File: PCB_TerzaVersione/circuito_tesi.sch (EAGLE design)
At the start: 57 parts, among them IC1 SCD41-D-R2, Q1 BSS138, Q2 BSS138, Q3 BSS138, Q4 BSS138, U3 MICS-6814, U6 BME280, U7 LIS3DH, Y1 ECS-.327-9-16-TR

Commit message: Colleganenti PCB fatti
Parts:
- removed U7: LIS3DH, LIS3DH:LIS3DH
- added U1: STMICROELECTRONICS_LIS3DHSTMICROELECTRONICS_LIS3DH_0_0, STMicroelectronics - LIS3DH:STMICROELECTRONICS_LIS3DHSTMICROELECTRONICS_LIS3DH_0_0
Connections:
- new net BATTERY: C9.1, MDBT42Q.P0.31/AIN7, R19.2, R20.2
- net 3.3V: now also U1.CS, U1.VDD, U1.VDD_IO; no longer U7.CS, U7.VDD, U7.VDD_IO
- net AIN4: no longer C9.1, R19.2, R20.2
- net GND: now also U1.1_GND, U1.2_GND, U1.RES, U1.SA0/SDO; no longer U7.GND, U7.GND1, U7.RES, U7.SDO/SA0
- net P8: no longer MDBT42Q.P0.25
- net SCL: now also U1.SCL/SPC; no longer U7.SCL/SPC
- net SDA: now also U1.SDA/SDI/SDO; no longer U7.SDA/SDI/SDO

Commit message: Connessioni OK
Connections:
- removed net AIN4: MDBT42Q.P0.28/AIN4
- net P8: now also MDBT42Q.P0.27
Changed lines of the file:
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@@
-</segment>
-</net>
-<net name="AIN4" class="0">
-<segment>
-<pinref part="MDBT42Q" gate="G$1" pin="P0.28/AIN4"/>
-<wire x1="-149.86" y1="25.4" x2="-134.62" y2="25.4" width="0.1524" layer="91"/>
-<label x="-134.62" y="25.4" size="1.778" layer="95" xref="yes"/>
 </segment>
 </net>
@@
 <label x="43.18" y="246.38" size="1.778" layer="95" rot="R180" xref="yes"/>
 </segment>
+<segment>
+<pinref part="MDBT42Q" gate="G$1" pin="P0.27"/>
+<wire x1="-149.86" y1="27.94" x2="-144.78" y2="27.94" width="0.1524" layer="91"/>
+<label x="-144.78" y="27.94" size="1.778" layer="95" xref="yes"/>
+</segment>
 </net>

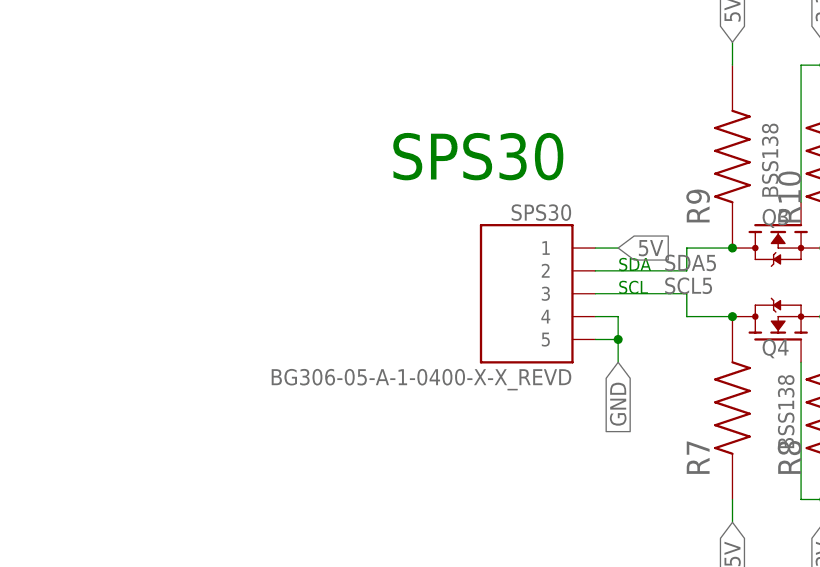
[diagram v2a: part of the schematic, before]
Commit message: Cambiato piedino SPS30
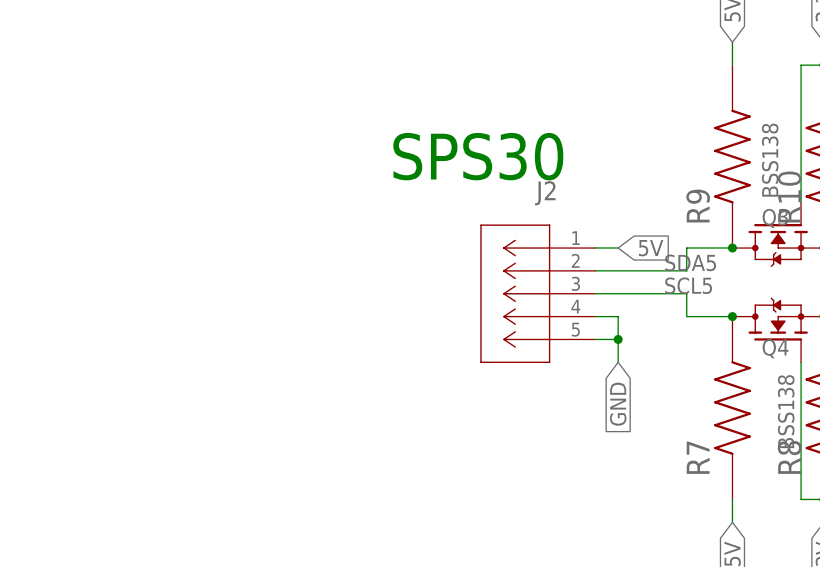
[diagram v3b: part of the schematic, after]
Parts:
- removed SPS30: BG306-05-A-1-0400-X-X_REVD, Connet_5_BG306-05-A-1-0400-X-X_REVD:BG306-05-A-1-0400-X-X_REVD
- added J2: S5B-ZR-SM4A-TF_(LF)_(SN)CONN_S5B-ZR-SM4A-TF_JST, CONN_SMD_5PIN:S5B-ZR-SM4A-TF_(LF)_(SN)CONN_S5B-ZR-SM4A-TF_JST
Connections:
- net 5V: now also J2.1; no longer SPS30.1
- net GND: now also J2.4, J2.5; no longer SPS30.4, SPS30.5
- net SCL5: now also J2.3; no longer SPS30.3
- net SDA5: now also J2.2; no longer SPS30.2
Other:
- note removed: "SCL"
- note removed: "SDA"
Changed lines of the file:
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@@
 <part name="GND1" library="SparkFun-PowerSymbols" deviceset="GND" device=""/>
 <part name="Y1" library="Crystal-ECS-.327-9-16-TR" deviceset="ECS-.327-9-16-TR" device=""/>
-<part name="SPS30" library="Connet_5_BG306-05-A-1-0400-X-X_REVD" deviceset="BG306-05-A-1-0400-X-X_REVD" device=""/>
 <part name="PROGRAMMER" library="Connet_6_BG306-04-A-1-0400-X-X_REVD" deviceset="BG306-04-A-1-0400-X-X_REVD" device=""/>
 <part name="GND3" library="supply" deviceset="GND" device=""/>
@@
 <part name="C13" library="Condensatore_case_0402" deviceset="C0402H102J5GACTU" device=""/>
 <part name="U1" library="STMicroelectronics - LIS3DH" deviceset="STMICROELECTRONICS_LIS3DH" device="STMICROELECTRONICS_LIS3DH_0_0"/>
+<part name="J2" library="CONN_SMD_5PIN" deviceset="S5B-ZR-SM4A-TF_(LF)_(SN)" device="CONN_S5B-ZR-SM4A-TF_JST"/>
 </parts>
 <sheets>
 <sheet>
 <plain>
-<text x="-302.26" y="200.66" size="1.4224" layer="91">SCL</text>
-<text x="-302.26" y="203.2" size="1.4224" layer="91">SDA</text>
 <text x="-231.902" y="220.472" size="5.08" layer="91">SCD41</text>
 <text x="-327.66" y="213.36" size="5.08" layer="91">SPS30</text>
@@
 <attribute name="VALUE" x="-236.210609375" y="50.790609375" size="1.781290625" layer="96" rot="R90"/>
 </instance>
-<instance part="SPS30" gate="G$1" x="-312.42" y="200.66" smashed="yes" rot="MR0">
-<attribute name="NAME" x="-307.34" y="208.788" size="1.778" layer="95" rot="MR0"/>
-<attribute name="VALUE" x="-307.34" y="190.5" size="1.778" layer="96" rot="MR0"/>
-</instance>
 <instance part="PROGRAMMER" gate="G$1" x="-358.14" y="-15.24" smashed="yes" rot="MR0">
 <attribute name="NAME" x="-353.051440625" y="-7.0983" size="1.781" layer="95" rot="MR0"/>
@@
 <instance part="U1" gate="G$0" x="-213.36" y="144.78" smashed="yes">
 <attribute name="NAME" x="-213.36" y="142.24" size="2.54" layer="95" align="top-left"/>
+</instance>
+<instance part="J2" gate="A" x="-304.8" y="205.74" smashed="yes" rot="MR0">
+<attribute name="NAME" x="-308.9646" y="211.0486" size="2.083" layer="95" ratio="6" rot="MR0"/>
 </instance>
 </instances>
@@
 <segment>
 <label x="-302.26" y="205.74" size="1.778" layer="95" xref="yes"/>
-<pinref part="SPS30" gate="G$1" pin="1"/>
 <wire x1="-304.8" y1="205.74" x2="-302.26" y2="205.74" width="0.1524" layer="91"/>
+<pinref part="J2" gate="A" pin="1"/>
 </segment>
 <segment>
@@
 <wire x1="-294.64" y1="203.2" x2="-294.64" y2="205.74" width="0.1524" layer="91"/>
 <wire x1="-294.64" y1="205.74" x2="-289.56" y2="205.74" width="0.1524" layer="91"/>
-<pinref part="SPS30" gate="G$1" pin="2"/>
 <label x="-297.18" y="203.2" size="1.778" layer="95"/>
 <pinref part="R9" gate="G$1" pin="1"/>
 <junction x="-289.56" y="205.74"/>
+<pinref part="J2" gate="A" pin="2"/>
 </segment>
 </net>
@@
 <wire x1="-302.26" y1="195.58" x2="-302.26" y2="193.04" width="0.1524" layer="91"/>
 <label x="-302.26" y="193.04" size="1.778" layer="95" rot="R270" xref="yes"/>
-<pinref part="SPS30" gate="G$1" pin="4"/>
 <wire x1="-304.8" y1="198.12" x2="-302.26" y2="198.12" width="0.1524" layer="91"/>
-<pinref part="SPS30" gate="G$1" pin="5"/>
 <wire x1="-304.8" y1="195.58" x2="-302.26" y2="195.58" width="0.1524" layer="91"/>
+<pinref part="J2" gate="A" pin="4"/>
+<pinref part="J2" gate="A" pin="5"/>
 </segment>
 <segment>
@@
 <wire x1="-294.64" y1="198.12" x2="-289.56" y2="198.12" width="0.1524" layer="91"/>
 <pinref part="Q4" gate="G$1" pin="D"/>
-<pinref part="SPS30" gate="G$1" pin="3"/>
 <label x="-297.18" y="200.66" size="1.778" layer="95"/>
 <pinref part="R7" gate="G$1" pin="2"/>
 <junction x="-289.56" y="198.12"/>
-</segment>
-</net>
+<pinref part="J2" gate="A" pin="3"/>
+</segment>
+</net>

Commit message: Prototipo finale
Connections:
- net 3.3V: now also C5.1, V_R_1.8.ON_/_OFF, V_R_1.8.VIN
- net VDD: no longer C5.1, V_R_1.8.ON_/_OFF, V_R_1.8.VIN
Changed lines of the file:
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@@
-</segment>
-<segment>
-<label x="35.56" y="-12.7" size="1.778" layer="95" rot="R180" xref="yes"/>
-<pinref part="V_R_1.8" gate="G$1" pin="VIN"/>
-<wire x1="45.72" y1="-12.7" x2="38.1" y2="-12.7" width="0.1524" layer="91"/>
-<pinref part="C5" gate="G$1" pin="1"/>
-<wire x1="38.1" y1="-12.7" x2="35.56" y2="-12.7" width="0.1524" layer="91"/>
-<junction x="38.1" y="-12.7"/>
 </segment>
 <segment>
@@
 <junction x="45.72" y="35.56"/>
 <label x="43.18" y="35.56" size="1.778" layer="95" rot="R180" xref="yes"/>
-</segment>
-<segment>
-<pinref part="V_R_1.8" gate="G$1" pin="ON_/_OFF"/>
-<wire x1="45.72" y1="-17.78" x2="45.72" y2="-20.32" width="0.1524" layer="91"/>
-<label x="45.72" y="-20.32" size="1.778" layer="95" rot="R270" xref="yes"/>
 </segment>
 <segment>
@@
 <wire x1="-220.98" y1="111.76" x2="-218.44" y2="111.76" width="0.1524" layer="91"/>
 </segment>
+<segment>
+<pinref part="V_R_1.8" gate="G$1" pin="VIN"/>
+<wire x1="45.72" y1="-12.7" x2="38.1" y2="-12.7" width="0.1524" layer="91"/>
+<pinref part="C5" gate="G$1" pin="1"/>
+<wire x1="38.1" y1="-12.7" x2="30.48" y2="-12.7" width="0.1524" layer="91"/>
+<junction x="38.1" y="-12.7"/>
+<label x="30.48" y="-12.7" size="1.778" layer="95" rot="R180" xref="yes"/>
+</segment>
+<segment>
+<pinref part="V_R_1.8" gate="G$1" pin="ON_/_OFF"/>
+<wire x1="45.72" y1="-17.78" x2="45.72" y2="-22.86" width="0.1524" layer="91"/>
+<label x="45.72" y="-22.86" size="1.778" layer="95" rot="R270" xref="yes"/>
+</segment>
 </net>

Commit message: Cambiato collegamento BJT
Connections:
- net 5V: now also OPAMP.VCC+, R11.1, R12.1; no longer BJT.C
- net BJT: now also BJT.C, U3.RH1/RS1_OX, U3.RH1/RS1_RED; no longer BJT.E, OPAMP.VCC+, R11.1, R12.1
- net GND: now also BJT.E; no longer U3.RH1/RS1_OX, U3.RH1/RS1_RED
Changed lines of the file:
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@@
 <part name="U1" library="STMicroelectronics - LIS3DH" deviceset="STMICROELECTRONICS_LIS3DH" device="STMICROELECTRONICS_LIS3DH_0_0"/>
 <part name="J2" library="CONN_SMD_5PIN" deviceset="S5B-ZR-SM4A-TF_(LF)_(SN)" device="CONN_S5B-ZR-SM4A-TF_JST"/>
+<part name="GND11" library="supply" deviceset="GND" device=""/>
 </parts>
 <sheets>
@@
 <attribute name="NAME" x="-308.9646" y="211.0486" size="2.083" layer="95" ratio="6" rot="MR0"/>
 </instance>
+<instance part="GND11" gate="1" x="83.82" y="236.22" smashed="yes">
+<attribute name="VALUE" x="81.28" y="233.68" size="1.778" layer="96"/>
+</instance>
 </instances>
 <busses>
@@
 </segment>
 <segment>
-<pinref part="BJT" gate="G$1" pin="C"/>
-<wire x1="83.82" y1="251.46" x2="83.82" y2="256.54" width="0.1524" layer="91"/>
-<label x="83.82" y="256.54" size="1.778" layer="95" rot="R90" xref="yes"/>
+<pinref part="OPAMP" gate="A" pin="VCC+"/>
+<wire x1="71.12" y1="200.66" x2="73.66" y2="200.66" width="0.1524" layer="91"/>
+<label x="73.66" y="200.66" size="1.778" layer="95" xref="yes"/>
+</segment>
+<segment>
+<pinref part="R11" gate="G$1" pin="1"/>
+<wire x1="170.18" y1="187.96" x2="172.72" y2="187.96" width="0.1524" layer="91"/>
+<label x="172.72" y="187.96" size="1.778" layer="95" xref="yes"/>
+</segment>
+<segment>
+<pinref part="R12" gate="G$1" pin="1"/>
+<wire x1="96.52" y1="226.06" x2="96.52" y2="228.6" width="0.1524" layer="91"/>
+<label x="96.52" y="228.6" size="1.778" layer="95" rot="R90" xref="yes"/>
 </segment>
 </net>
@@
 <wire x1="71.12" y1="182.88" x2="73.66" y2="182.88" width="0.1524" layer="91"/>
 <label x="73.66" y="182.88" size="1.778" layer="95" xref="yes"/>
-</segment>
-<segment>
-<pinref part="U3" gate="G$1" pin="RH1/RS1_RED"/>
-<wire x1="147.32" y1="203.2" x2="149.86" y2="203.2" width="0.1524" layer="91"/>
-<label x="149.86" y="203.2" size="1.778" layer="95" xref="yes"/>
-</segment>
-<segment>
-<pinref part="U3" gate="G$1" pin="RH1/RS1_OX"/>
-<wire x1="101.6" y1="187.96" x2="99.06" y2="187.96" width="0.1524" layer="91"/>
-<label x="99.06" y="187.96" size="1.778" layer="95" rot="R180" xref="yes"/>
 </segment>
 <segment>
@@
 <junction x="-180.34" y="114.3"/>
 </segment>
+<segment>
+<pinref part="BJT" gate="G$1" pin="E"/>
+<wire x1="83.82" y1="241.3" x2="83.82" y2="238.76" width="0.1524" layer="91"/>
+<pinref part="GND11" gate="1" pin="GND"/>
+</segment>
 </net>
 <net name="N$11" class="0">
@@
 <junction x="-241.3" y="50.8"/>
 <pinref part="C13" gate="G$1" pin="1"/>
-</segment>
-</net>
-<net name="BJT" class="0">
-<segment>
-<pinref part="BJT" gate="G$1" pin="E"/>
-<wire x1="83.82" y1="241.3" x2="83.82" y2="238.76" width="0.1524" layer="91"/>
-<label x="83.82" y="238.76" size="1.778" layer="95" rot="R270" xref="yes"/>
-</segment>
-<segment>
-<pinref part="R12" gate="G$1" pin="1"/>
-<wire x1="96.52" y1="226.06" x2="96.52" y2="228.6" width="0.1524" layer="91"/>
-<label x="96.52" y="228.6" size="1.778" layer="95" rot="R90" xref="yes"/>
-</segment>
-<segment>
-<pinref part="R11" gate="G$1" pin="1"/>
-<wire x1="170.18" y1="187.96" x2="172.72" y2="187.96" width="0.1524" layer="91"/>
-<label x="172.72" y="187.96" size="1.778" layer="95" xref="yes"/>
-</segment>
-<segment>
-<pinref part="OPAMP" gate="A" pin="VCC+"/>
-<wire x1="71.12" y1="200.66" x2="73.66" y2="200.66" width="0.1524" layer="91"/>
-<label x="73.66" y="200.66" size="1.778" layer="95" xref="yes"/>
 </segment>
 </net>
@@
 </segment>
 </net>
+<net name="BJT" class="0">
+<segment>
+<pinref part="U3" gate="G$1" pin="RH1/RS1_RED"/>
+<wire x1="147.32" y1="203.2" x2="149.86" y2="203.2" width="0.1524" layer="91"/>
+<label x="149.86" y="203.2" size="1.778" layer="95" xref="yes"/>
+</segment>
+<segment>
+<pinref part="U3" gate="G$1" pin="RH1/RS1_OX"/>
+<wire x1="101.6" y1="187.96" x2="99.06" y2="187.96" width="0.1524" layer="91"/>
+<label x="99.06" y="187.96" size="1.778" layer="95" rot="R180" xref="yes"/>
+</segment>
+<segment>
+<pinref part="BJT" gate="G$1" pin="C"/>
+<wire x1="83.82" y1="251.46" x2="83.82" y2="254" width="0.1524" layer="91"/>
+<label x="83.82" y="254" size="1.778" layer="95" rot="R90" xref="yes"/>
+</segment>
+</net>

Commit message: Resistenze con valore esatto
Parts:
- removed LED1: LTST-C170TBKT, LED_0805:LTST-C170TBKT
- added LED: LTST-C170KRKT, LED_R_LTST-C170KRKT:LTST-C170KRKT
- R1, R10, R2, R3, R4, R5, R6, R7, R8, R9: value 8-1879333-9 -> MCS0402MC1002FE000; device Resistenza_case_0402:8-1879333-9 -> Res_10K_0402:MCS0402MC1002FE000
- R11: value 8-1879333-9 -> ERJPA2F1300X; device Resistenza_case_0402:8-1879333-9 -> Res_130_0402:ERJPA2F1300X
- R12: value 8-1879333-9 -> ERJPA2J821X; device Resistenza_case_0402:8-1879333-9 -> Res_820_0402:ERJPA2J821X
- R13, R14, R19, R20: value 8-1879333-9 -> ERJ-2GEJ515X; device Resistenza_case_0402:8-1879333-9 -> Res_5,1M_0402:ERJ-2GEJ515X
- R15, R16: value 8-1879333-9 -> ERJ-2GEJ106X; device Resistenza_case_0402:8-1879333-9 -> Res_10M_0402:ERJ-2GEJ106X
- R17: value 8-1879333-9 -> ERJPA2F5101X; device Resistenza_case_0402:8-1879333-9 -> Res_5,1K_0402:ERJPA2F5101X
- R18: value 8-1879333-9 -> ERA2AEB331X; device Resistenza_case_0402:8-1879333-9 -> Res_330_0402:ERA2AEB331X
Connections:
- net 5V: now also R11.2, R12.2; no longer R11.1, R12.1
- net LED: now also LED.+; no longer LED1.+
- net N$11: now also R12.1; no longer R12.2
- net N$13: now also R11.1; no longer R11.2
- net N$9: now also LED.-; no longer LED1.-
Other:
- moved on the sheet: R11, R12

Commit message: Messi condensatori corretti
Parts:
- added JP1: (no value), pinhead:PINHD-1X4
- C1, C10, C2: value C0402H102J5GACTU -> C0402C104K9RACAUTO; device Condensatore_case_0402:C0402H102J5GACTU -> Cond_100n_0402:C0402C104K9RACAUTO
- C11: value C0402H102J5GACTU -> CL05A106MP5NUNC; device Condensatore_case_0402:C0402H102J5GACTU -> Cond_10u_0402:CL05A106MP5NUNC
- C12, C13: value C0402H102J5GACTU -> 04025A120FAT2A; device Condensatore_case_0402:C0402H102J5GACTU -> Cond_12p_0402:04025A120FAT2A
- C3: value C0402H102J5GACTU -> CL05A225MQ5NNNC; device Condensatore_case_0402:C0402H102J5GACTU -> Cond_2,2u_0402:CL05A225MQ5NNNC
- C4: value C0402H102J5GACTU -> CL05B471KB5NNNCCAP_CL05_SAM; device Condensatore_case_0402:C0402H102J5GACTU -> Cond_470p_0402:CL05B471KB5NNNCCAP_CL05_SAM
- C5, C6: value C0402H102J5GACTU -> JMK105BJ105KV-F; device Condensatore_case_0402:C0402H102J5GACTU -> Cond_1u_0402:JMK105BJ105KV-F
- C7, C8, C9: value C0402H102J5GACTU -> CL05B103KO5NNNC; device Condensatore_case_0402:C0402H102J5GACTU -> Cond_10n_0402:CL05B103KO5NNNC
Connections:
- net 1.8V: now also C6.2; no longer C6.1
- net 3.3V: now also C5.2; no longer C5.1
- net GND: now also C12.1, C13.1, C4.1, C5.1, C6.1; no longer C12.2, C13.2, C4.2, C5.2, C6.2
- net N$14: now also C4.2; no longer C4.1
- net N$17: now also C12.2; no longer C12.1
- net N$18: now also C13.2; no longer C13.1

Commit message: Sistemati dei dettagli
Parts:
- removed JP1: (no value), pinhead:PINHD-1X4
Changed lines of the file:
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@@
 <part name="R19" library="Res_5,1M_0402" deviceset="ERJ-2GEJ515X" device=""/>
 <part name="R20" library="Res_5,1M_0402" deviceset="ERJ-2GEJ515X" device=""/>
-<part name="JP1" library="pinhead" library_urn="urn:adsk.eagle:library:325" deviceset="PINHD-1X4" device="" package3d_urn="urn:adsk.eagle:package:22407/2"/>
 <part name="C1" library="Cond_100n_0402" deviceset="C0402C104K9RACAUTO" device=""/>
 <part name="C2" library="Cond_100n_0402" deviceset="C0402C104K9RACAUTO" device=""/>
@@
 <attribute name="NAME" x="50.79851875" y="-83.824440625" size="2.54148125" layer="95" rot="R90"/>
 </instance>
-<instance part="JP1" gate="A" x="-114.3" y="127" smashed="yes">
-<attribute name="NAME" x="-120.65" y="135.255" size="1.778" layer="95"/>
-<attribute name="VALUE" x="-120.65" y="119.38" size="1.778" layer="96"/>
-</instance>
 <instance part="C1" gate="G$1" x="48.26" y="66.04" smashed="yes" rot="R90">
 <attribute name="NAME" x="44.45" y="66.04" size="1.778" layer="95" rot="R90"/>
@@
 which will not be processed correctly with this version.
 </note>
-<note version="8.2" severity="warning">
-Since Version 8.2, EAGLE supports online libraries. The ids
-of those online libraries will not be understood (or retained)
-with this version.
-</note>
-<note version="8.3" severity="warning">
-Since Version 8.3, EAGLE supports URNs for individual library
-assets (packages, symbols, and devices). The URNs of those assets
-will not be understood (or retained) with this version.
-</note>
-<note version="8.3" severity="warning">
-Since Version 8.3, EAGLE supports the association of 3D packages
-with devices in libraries, schematics, and board files. Those 3D
-packages will not be understood (or retained) with this version.
-</note>
 </compatibility>
